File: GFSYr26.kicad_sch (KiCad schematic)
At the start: 44 parts

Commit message: BiProp 26 GFS Update
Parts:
- removed Needle_Valve3: ~, symbol PID_symbols:Needle_Valve
- added MB_FuelFill: ~, symbol PID_symbols:MBallValve
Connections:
- net at PT4.: now also Adj_ChokeN2., Hose_FillN2., Needle_Valve_Vent.
- net at PT1.: now also 1., BV_Fill1., Needle_Valve1.
- net at N2O_QD.: now also 1.
- net at 1.: now also CV1., CV2., PT3., Pmatic_VentVehicle., Relief_ValveN2O.; no longer N2O_QD.
- net at Manual_Pressure_Gauge1.: now also Filter1., N2O_1.
- net at Fuel.: now also MB_FuelFill.
- net at 1.: now also FuelVehicle.
- net at FuelVehicle.: no longer 1.
- new net: 1., N2_QD.
- new net: Filter2., Manual_Pressure_Gauge2., N2O_2.
- new net: 11., BV_Fill2., Needle_Valve2., PT2.
- new net: 1., MB_FuelFill.
- now unconnected: Manual_Pressure_Gauge2., Needle_Valve1., Needle_Valve2., Needle_Valve_Vent., PT2., PT3., Relief_ValveN2O.
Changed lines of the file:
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@@
 	)
 	(symbol
-		(lib_name "Needle_Valve_2")
-		(lib_id "PID_symbols:Needle_Valve")
-		(at 199.39 92.71 90)
+		(lib_name "MBallValve_2")
+		(lib_id "PID_symbols:MBallValve")
+		(at 199.39 88.9 90)
 		(unit 1)
 		(exclude_from_sim no)
@@
 		(on_board yes)
 		(dnp no)
-		(fields_autoplaced yes)
-		(property "Reference" "Needle_Valve3"
-			(at 203.2 87.6299 90)
+		(property "Reference" "MB_FuelFill"
+			(at 202.438 88.9 90)
 			(effects
 				(font
@@
 		)
 		(property "Footprint" ""
-			(at 199.39 92.71 0)
+			(at 199.39 88.9 0)
 			(effects
 				(font
@@
 		)
 		(property "Datasheet" ""
-			(at 199.39 92.71 0)
+			(at 199.39 88.9 0)
 			(effects
 				(font
@@
 		)
 		(property "Description" ""
-			(at 199.39 92.71 0)
+			(at 199.39 88.9 0)
 			(effects
 				(font
@@
 		)
 		(instances
-			(project ""
+			(project "P_IDs"
 				(path "/045f1f05-3134-4b6d-91b6-463031104f1e/a0b6300e-76e9-4a18-afd6-e2d656b0d8f9/0af49a0b-311a-4e5f-a192-08c30979a0d0"
-					(reference "Needle_Valve3")
+					(reference "MB_FuelFill")
 					(unit 1)
 				)

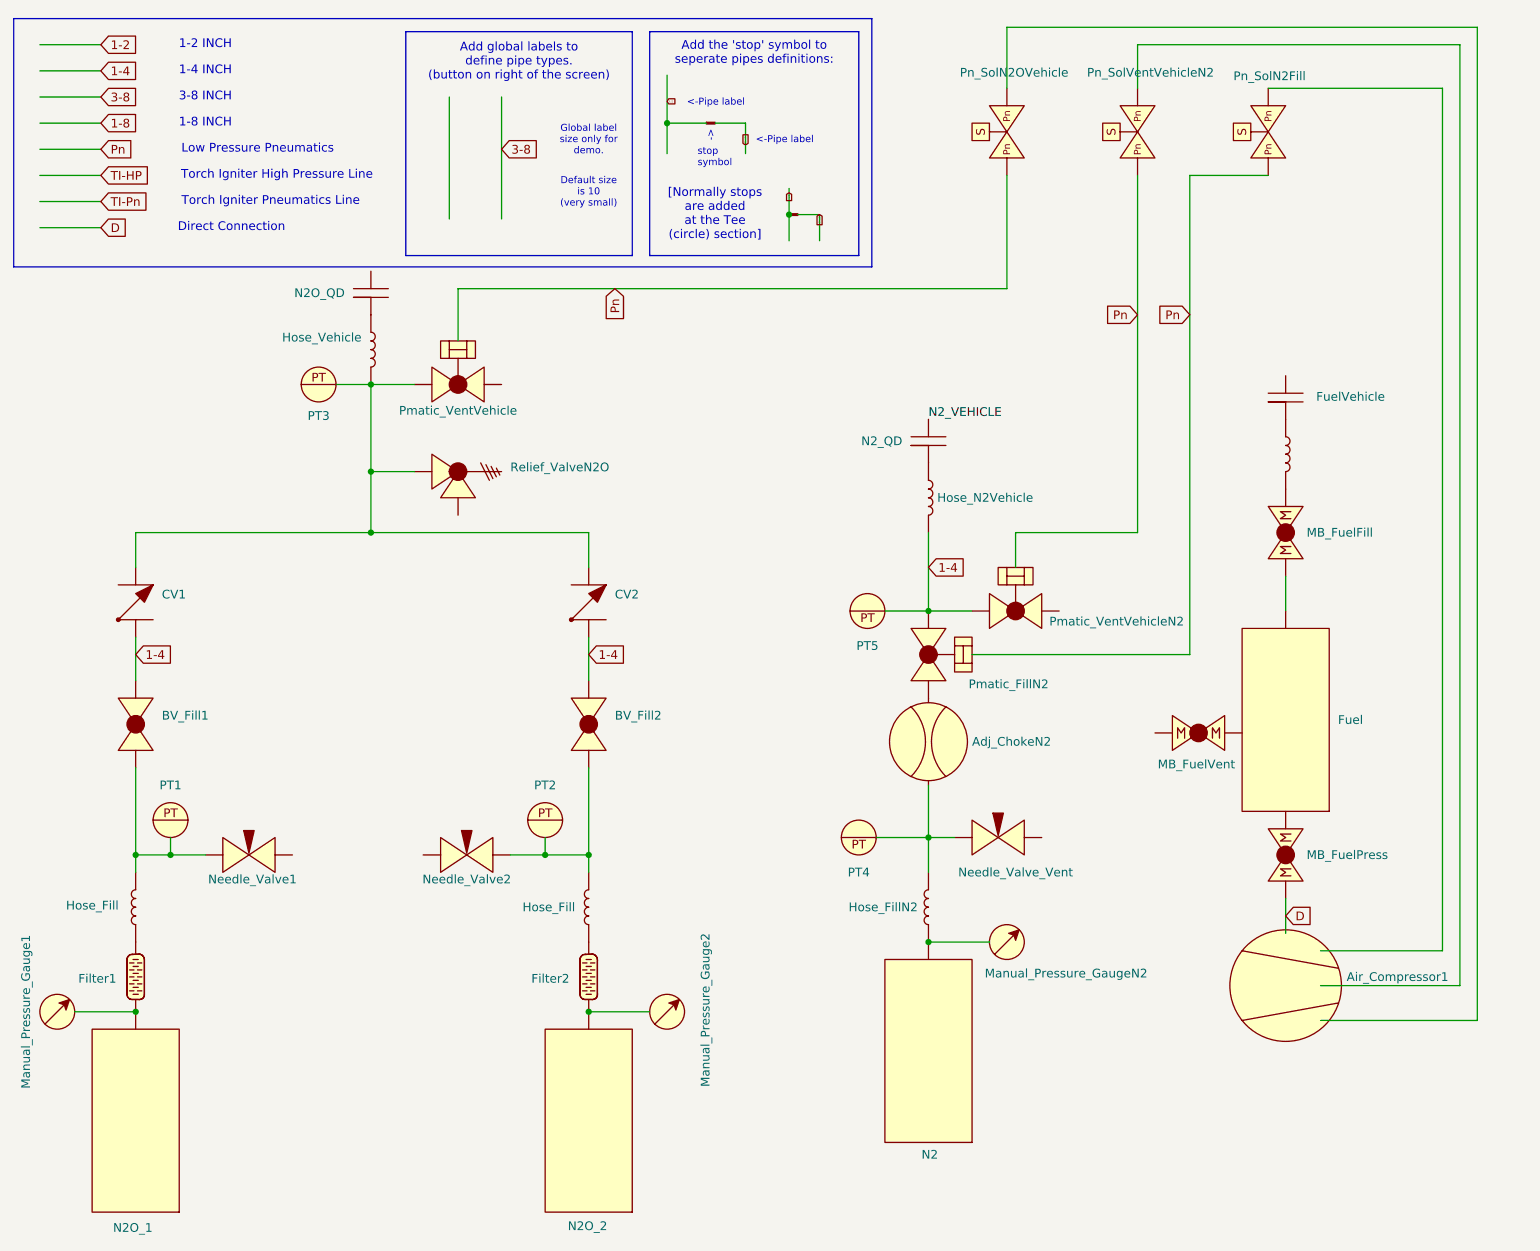
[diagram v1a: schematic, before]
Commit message: Added solenoids to gfs
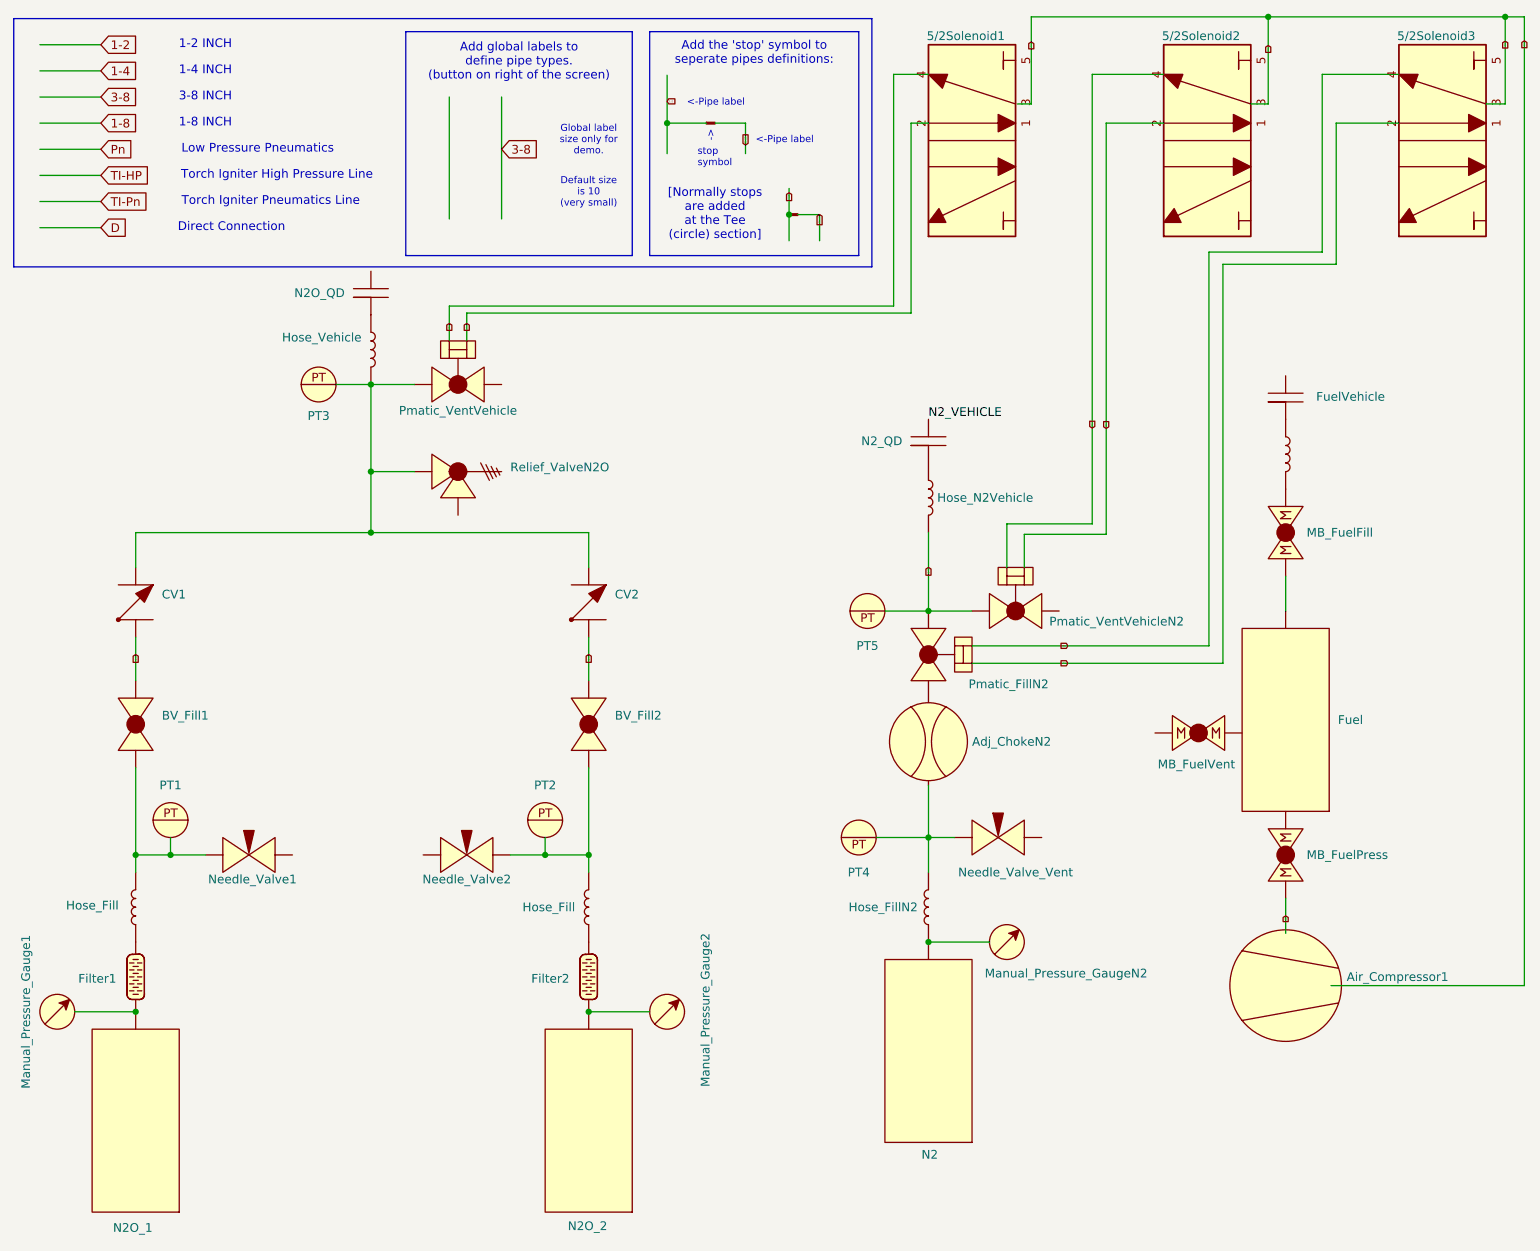
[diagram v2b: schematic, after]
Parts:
- removed Pn_SolN2Fill, Pn_SolN2OVehicle, Pn_SolVentVehicleN2: ~, symbol PID_symbols:Pneumatic_Solenoid
- added 5/2Solenoid1, 5/2Solenoid2, 5/2Solenoid3: ~, symbol PID_symbols:Solenoid_5/2
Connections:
- net Pn: now also 5/2Solenoid1., 5/2Solenoid2., 5/2Solenoid3.; no longer Pmatic_FillN2., Pmatic_VentVehicle., Pmatic_VentVehicleN2.
- net at PT4.: now also Adj_ChokeN2., Hose_FillN2., Needle_Valve_Vent.
- net at PT1.: now also 1., BV_Fill1., Needle_Valve1.
- net at N2O_QD.: now also 1.
- net at 1.: now also CV1., CV2., PT3., Pmatic_VentVehicle., Relief_ValveN2O.; no longer N2O_QD.
- net at Manual_Pressure_Gauge1.: now also Filter1., N2O_1.
- new net: 1., N2_QD.
- new net: Filter2., Manual_Pressure_Gauge2., N2O_2.
- new net: 11., BV_Fill2., Needle_Valve2., PT2.
- now unconnected: Manual_Pressure_Gauge2., Needle_Valve1., Needle_Valve2., Needle_Valve_Vent., PT2., PT3., Pmatic_VentVehicle., Relief_ValveN2O.
